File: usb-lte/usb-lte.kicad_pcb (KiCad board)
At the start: 4 copper layers, 26 x 45 mm, 64 parts, among them J1 Sim slot, J2 Conn_Coaxial, J3 Conn_Coaxial, J4 Conn_Coaxial, P1 USB_C_Plug_USB2.0, Q1 BC847W, Q2 BC847W, U1 TPS62A02APDDC, U2 EG95

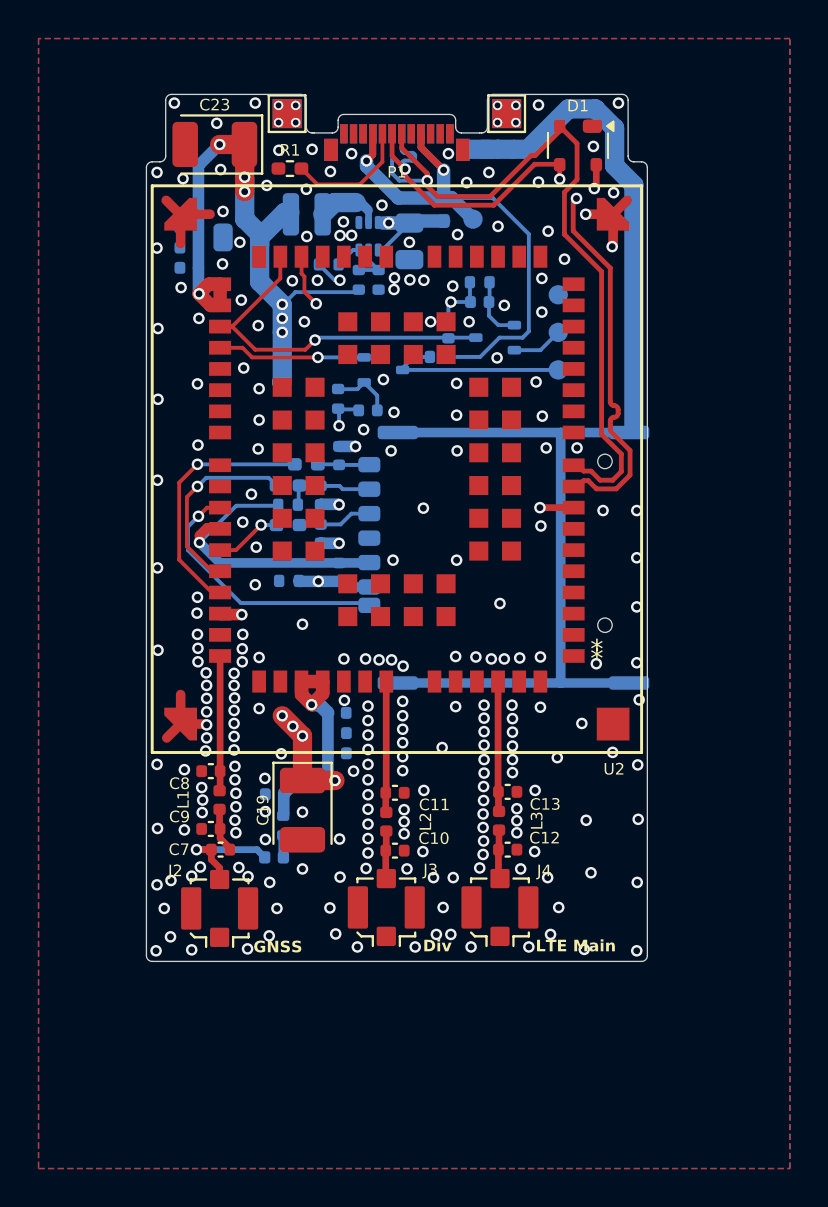
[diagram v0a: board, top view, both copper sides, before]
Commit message: Add TVS diode for sim slot
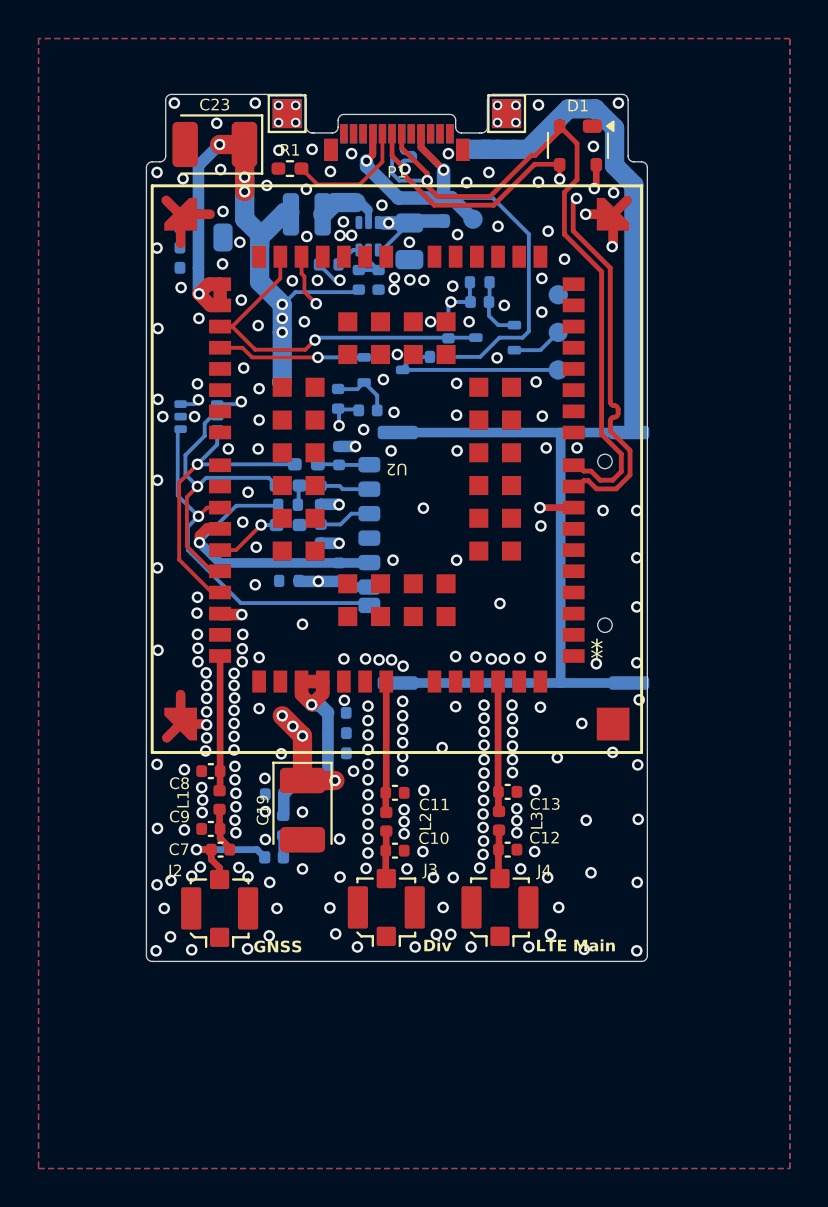
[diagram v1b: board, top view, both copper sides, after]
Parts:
- added D2: SMF05C, Package_TO_SOT_SMD:SOT-363_SC-70-6, B.Cu at (140.3, 105.6)
- R4: value 0 -> 0R
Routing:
- net MODEM_USIM_VDD: track 15.5 -> 24.6 mm, vias 1 -> 2
- net MODEM_USIM_RST: track 3.47 -> 11.6 mm, vias 1 -> 2
- net MODEM_USIM_PRESENCE: track 13.9 -> 18.9 mm
- net MODEM_USIM_DATA: track 10.5 -> 15.2 mm
- net MODEM_USIM_CLK: track 13.2 -> 15.5 mm
- net GND: vias 249 -> 252

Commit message: Moved TVS diode closer to sim slot
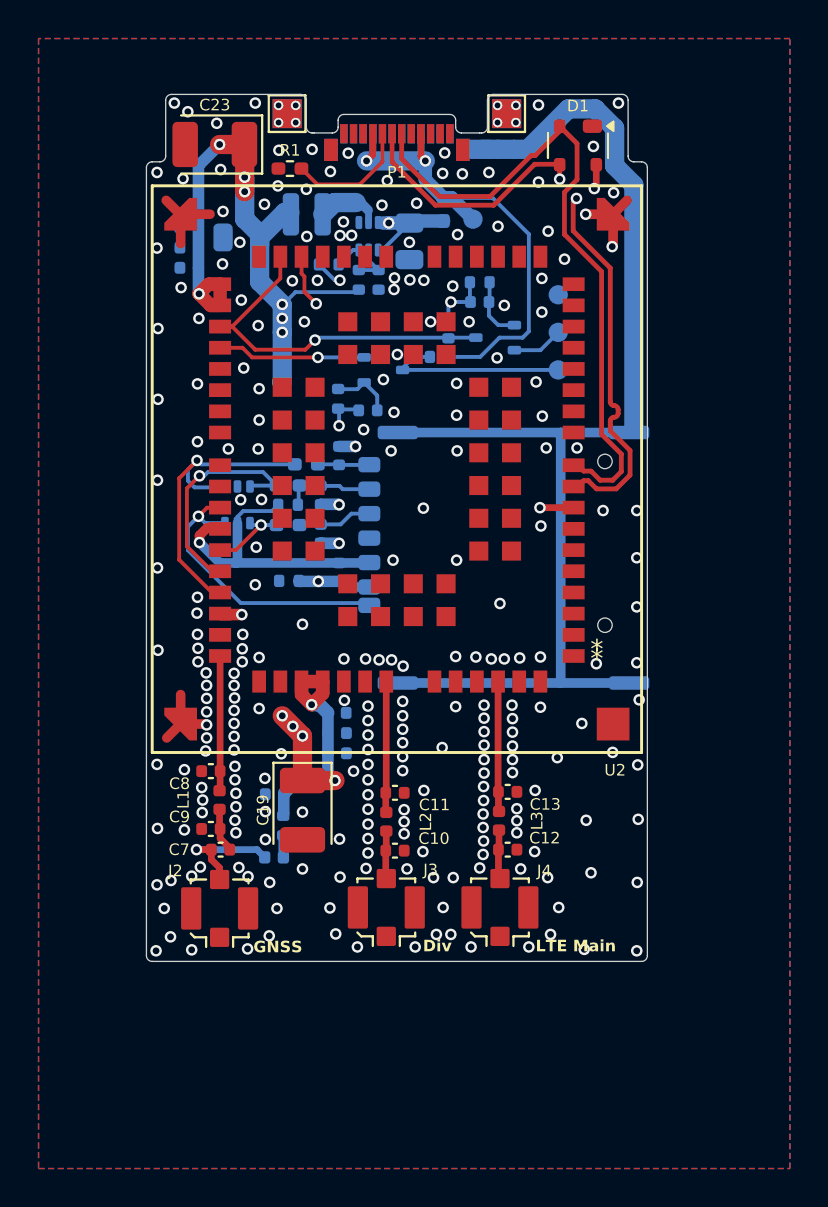
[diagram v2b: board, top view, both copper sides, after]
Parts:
- moved D2 4.99 mm to (142.3, 110.2), turned to -90 degrees
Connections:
- D2 pad 1: MODEM_USIM_PRESENCE -> MODEM_USIM_CLK
- D2 pad 3: MODEM_USIM_VDD -> MODEM_USIM_DATA
- D2 pad 5: MODEM_USIM_DATA -> MODEM_USIM_VDD
- D2 pad 6: MODEM_USIM_CLK -> MODEM_USIM_PRESENCE
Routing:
- net MODEM_USIM_VDD: track 24.6 -> 15.6 mm, vias 2 -> 1
- net MODEM_USIM_RST: track 11.6 -> 4.08 mm, vias 2 -> 1
- net USB_DN: track 38.6 -> 34.5 mm, vias 1 -> 0
- net MODEM_USIM_PRESENCE: track 18.9 -> 15.4 mm
- net USB_DP: track 36.5 -> 33.5 mm, vias 3 -> 2
- net MODEM_USIM_DATA: track 15.2 -> 12.4 mm
- net MODEM_USIM_CLK: track 15.5 -> 16.9 mm
- net VBUS: track 62.4 -> 61.5 mm
- net GND: vias 252 -> 256

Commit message: Add debug uart breakout
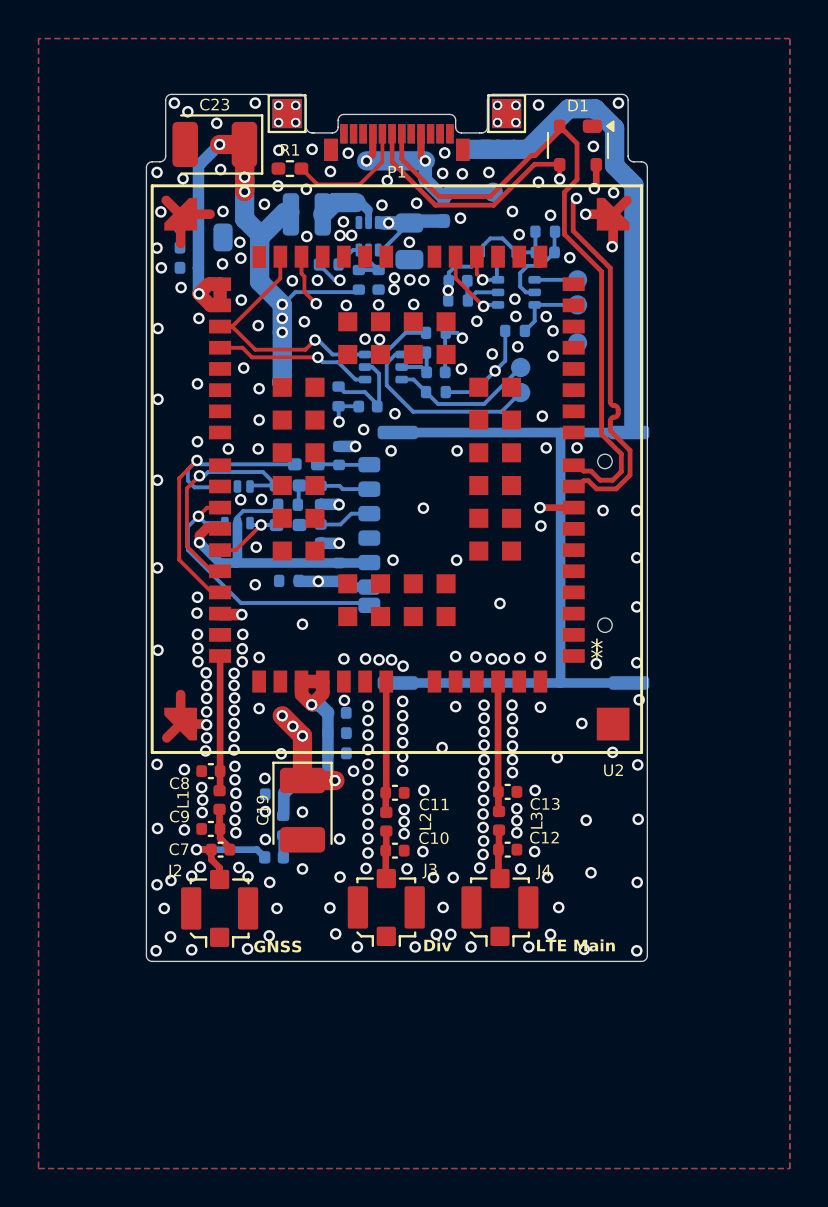
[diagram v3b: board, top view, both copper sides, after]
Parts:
- added C25: 1uF, Capacitor_SMD:C_0402_1005Metric, B.Cu at (153.8, 98.6)
- added C26: 1uF, Capacitor_SMD:C_0402_1005Metric, B.Cu at (158.3, 97.1)
- added R17: 4.7k, Resistor_SMD:R_0402_1005Metric, B.Cu at (153.8, 99.6)
- added R18: 10k, Resistor_SMD:R_0402_1005Metric, B.Cu at (156.7, 101.2)
- added R19: 10k, Resistor_SMD:R_0402_1005Metric, B.Cu at (156.3, 97.1)
- added R20: 4.7k, Resistor_SMD:R_0402_1005Metric, B.Cu at (158.3, 96.0)
- added TP10: TestPoint, footprints:TestPoint_Pad_1mm, B.Cu at (160.0, 99.8)
- added TP11: TestPoint, footprints:TestPoint_Pad_1mm, B.Cu at (160.0, 98.5)
- Q1, Q2: value BC847W -> MBT3904DW1; footprint Package_TO_SOT_SMD:SOT-323_SC-70 -> Package_TO_SOT_SMD:SOT-363_SC-70-6
- moved C15 4.30 mm to (152.6, 103.3), turned to 0 degrees
- moved R12 4.30 mm to (152.6, 102.3), turned to 0 degrees
- moved TP6 3.68 mm to (157.0, 104.4)
- moved TP7 2.69 mm to (160.0, 101.8)
- moved Q2 2.59 mm to (156.8, 99.2), turned to 0 degrees
- moved TP5 1.95 mm to (157.0, 103.1)
- moved R9 1.84 mm to (152.6, 104.3)
- moved TP8 1.75 mm to (155.6, 94.0)
- moved R10 0.69 mm to (152.6, 101.3), turned to 0 degrees
- moved C14 0.20 mm to (149.1, 105.1)
- moved Q1 0.15 mm to (149.9, 103.0)
- moved R11 0.13 mm to (147.6, 104.6)
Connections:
- C14 pad 2: Net-(Q1-B) -> Net-(Q1A-B1)
- C15 pad 1: Net-(Q2-B) -> Net-(Q1B-B2)
- Q1 pad 1: Net-(Q1-B) -> UART_TX_1V8
- Q1 pad 2: UART_TX_1V8 -> Net-(Q1A-B1)
- Q1 pad 3: UART_TX_5V -> UART_RX_1V8
- Q2 pad 1: Net-(Q2-B) -> DEBUG_TX_1V8
- Q2 pad 2: UART_RX_5V -> Net-(Q2A-B1)
- Q2 pad 3: UART_RX_1V8 -> DEBUG_RX_1V8
- R11 pad 2: Net-(Q1-B) -> Net-(Q1A-B1)
- R12 pad 1: Net-(Q2-B) -> Net-(Q1B-B2)
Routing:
- net VDD_EXT: track 21.6 -> 32.0 mm, vias 3 -> 4
- net UART_RX_5V: track 2.66 -> 10.0 mm
- net Net-(Q1A-B1): track 0.00 -> 5.11 mm
- net Net-(Q2B-B2): track 0.00 -> 4.89 mm
- net DEBUG_TX_1V8: track 0.00 -> 3.96 mm, vias 0 -> 1
- net VBUS: track 61.5 -> 57.7 mm, vias 4 -> 5
- net DEBUG_TX_5V: track 0.00 -> 3.78 mm
- net DEBUG_RX_1V8: track 0.00 -> 3.57 mm, vias 0 -> 1
- net Net-(Q2-B): track 3.28 -> 0.00 mm
- net Net-(Q1-B): track 3.23 -> 0.00 mm
- net Net-(Q2A-B1): track 0.00 -> 2.78 mm
- net Net-(Q1B-B2): track 0.00 -> 2.45 mm
- net UART_TX_5V: track 9.83 -> 7.49 mm
- net DEBUG_RX_5V: track 0.00 -> 2.22 mm
- net UART_RX_1V8: track 19.3 -> 17.5 mm
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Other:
- board text added: "Debug UART"
- board text added: "Main UART"
- board text removed: "UART 5V"

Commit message: Add various test points
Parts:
- added TP12: TestPoint, footprints:TestPoint_Pad_1mm, B.Cu at (161.9, 130.8)
- added TP13: TestPoint, footprints:TestPoint_Pad_1mm, B.Cu at (161.9, 128.8)
- added TP14: TestPoint, footprints:TestPoint_Pad_1mm, B.Cu at (161.9, 124.8)
- added TP15: TestPoint, footprints:TestPoint_Pad_1mm, B.Cu at (161.9, 126.8)
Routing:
- net MODEM_NETLIGHT: track 0.00 -> 37.5 mm, vias 0 -> 2
- net MODEM_PWRKEY: track 0.00 -> 36.0 mm, vias 0 -> 2
- net MODEM_RESET: track 0.00 -> 35.1 mm, vias 0 -> 2
- net MODEM_STATUS: track 0.00 -> 34.7 mm, vias 0 -> 2
- net VBUS: track 57.7 -> 61.2 mm
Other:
- board text added: "Network"
- board text added: "Power key"
- board text added: "Reset"
- board text added: "Status"

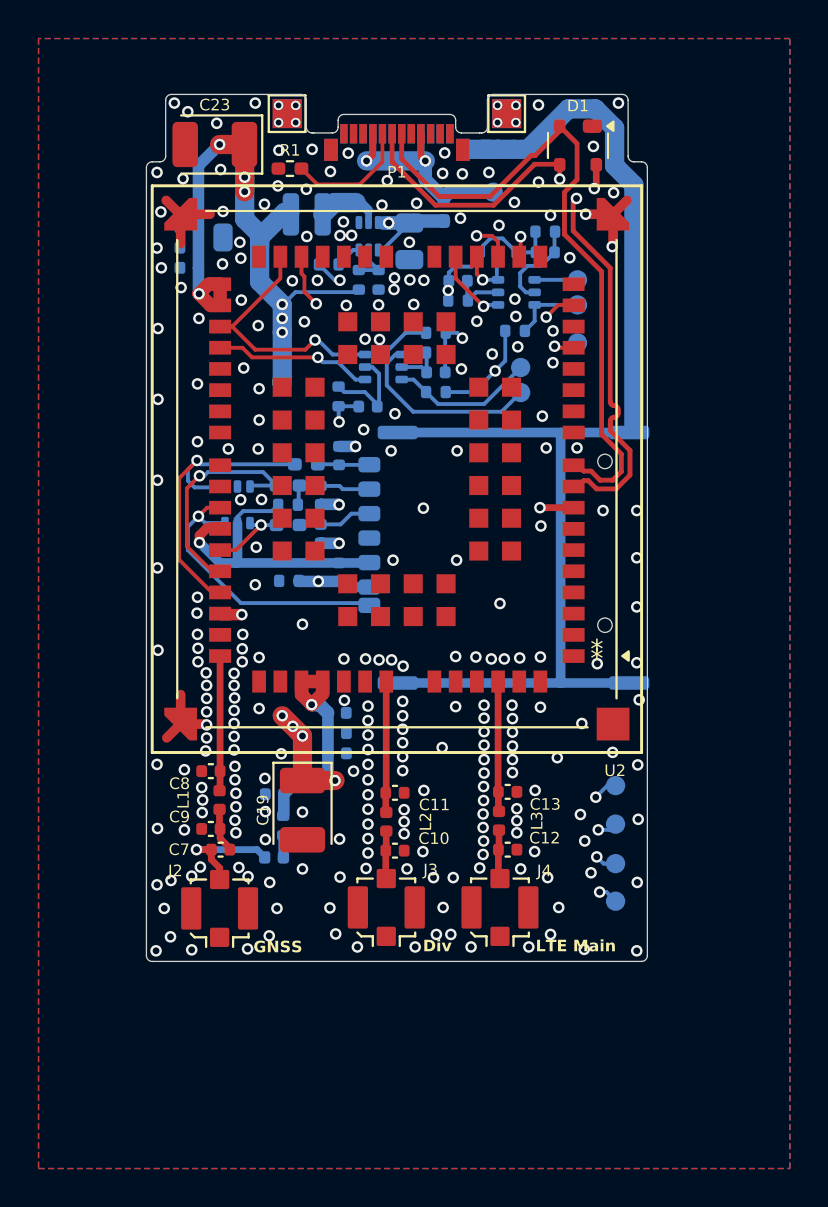
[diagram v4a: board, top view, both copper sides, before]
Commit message: Add status lights and usb boot key
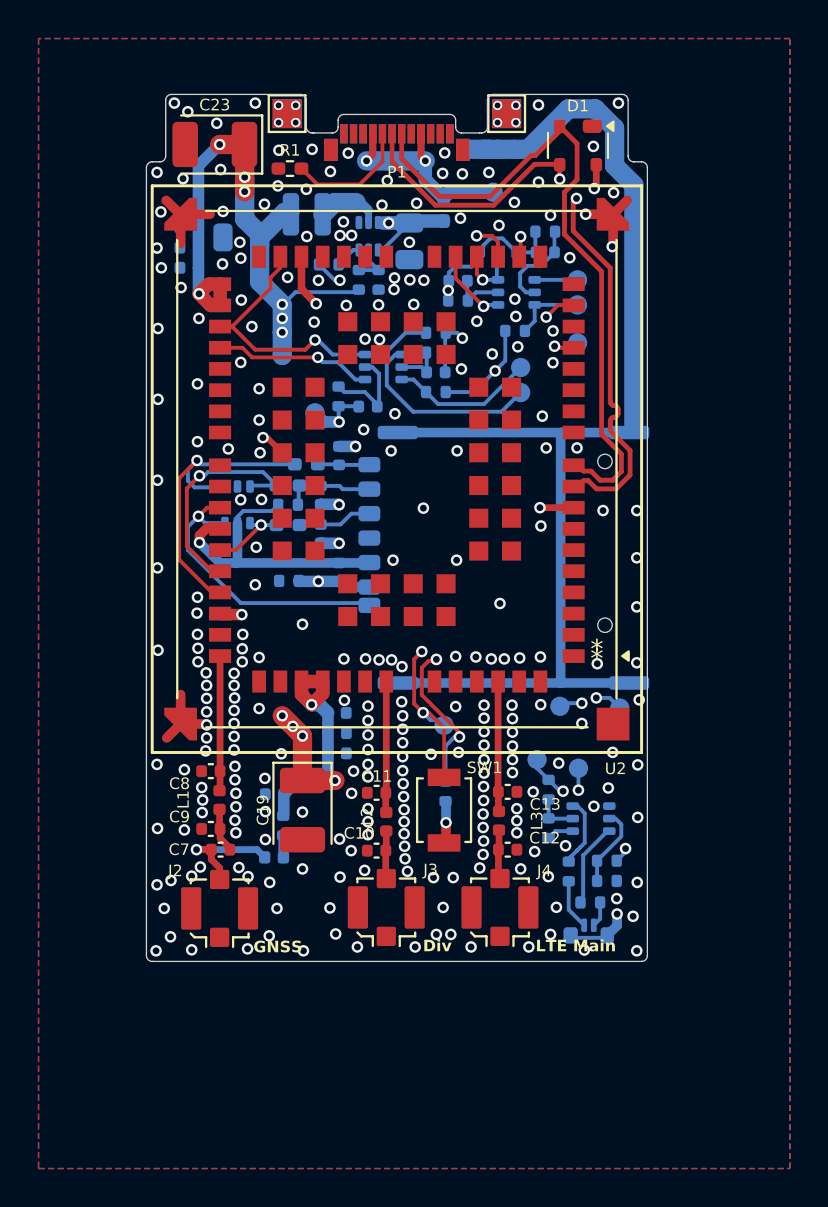
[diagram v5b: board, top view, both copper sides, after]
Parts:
- added D3: LED_Dual_AKKA, footprints:LED_Dual_0805_4pin, B.Cu at (160.6, 132.6)
- added Q3: MBT3904DW1, Package_TO_SOT_SMD:SOT-363_SC-70-6, B.Cu at (160.7, 126.5)
- added R21: 4.7k, Resistor_SMD:R_0402_1005Metric, B.Cu at (159.5, 129.2)
- added R22: 4.7k, Resistor_SMD:R_0402_1005Metric, B.Cu at (160.6, 130.8)
- added R23: 4.7k, Resistor_SMD:R_0402_1005Metric, B.Cu at (161.5, 128.7)
- added R24: 4.7k, Resistor_SMD:R_0402_1005Metric, B.Cu at (158.5, 125.0)
- added R25: 47k, Resistor_SMD:R_0402_1005Metric, B.Cu at (161.5, 129.7)
- added R26: 47k, Resistor_SMD:R_0402_1005Metric, B.Cu at (158.5, 127.0)
- added R27: 4.7k, Resistor_SMD:R_0402_1005Metric, B.Cu at (153.1, 125.1)
- added SW1: B3U-1000P, Button_Switch_SMD:SW_SPST_B3U-1000P, F.Cu at (153.1, 126.0)
- added TP16: TestPoint, footprints:TestPoint_Pad_1mm, B.Cu at (146.3, 105.4)
- added TP17: TestPoint, footprints:TestPoint_Pad_1mm, B.Cu at (153.1, 121.7)
- R2: value 15K -> 15k
- moved TP12 10.0 mm to (162.2, 120.8)
- moved TP13 8.66 mm to (159.1, 120.7)
- moved TP15 5.28 mm to (157.9, 123.4)
- moved TP14 2.12 mm to (160.0, 123.9)
- moved TP9 1.40 mm to (144.7, 102.5)
- moved C10 0.96 mm to (149.5, 128.2), turned to 180 degrees
- moved C11 0.96 mm to (149.5, 125.2), turned to 180 degrees
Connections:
- U2 pad 75: unconnected-(U2B-USB_BOOT-Pad75) -> MODEM_USB_BOOT
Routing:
- net MODEM_USB_BOOT: track 0.00 -> 41.4 mm, vias 0 -> 3
- net VDD: track 73.9 -> 102.2 mm, vias 12 -> 13
- net VDD_EXT: track 32.0 -> 56.0 mm, vias 4 -> 6
- net MODEM_PWRKEY: track 36.0 -> 25.4 mm
- net MODEM_RESET: track 35.1 -> 26.2 mm
- net MODEM_STATUS: track 34.7 -> 39.2 mm, vias 2 -> 3
- net Net-(Q3B-C2): track 0.00 -> 4.38 mm
- net Net-(Q3A-B1): track 0.00 -> 4.21 mm
- net Net-(Q3A-C1): track 0.00 -> 3.63 mm
- net Net-(D3-K2): track 0.00 -> 2.62 mm
- net Net-(Q3B-B2): track 0.00 -> 2.24 mm
- net Net-(R27-Pad1): track 0.00 -> 2.22 mm, vias 0 -> 1
- net GND: track 13.2 -> 14.6 mm, vias 262 -> 268
- net Net-(D3-K1): track 0.00 -> 1.32 mm
- net MODEM_NETLIGHT: track 37.5 -> 36.3 mm
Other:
- board text added: "1.8V"
- board text added: "Boot"
